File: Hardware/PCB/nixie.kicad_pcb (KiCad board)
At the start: 4 copper layers, 241.3 x 116.8 mm, 329 parts, among them J101 USB_B, J102 Conn_01x10, J103 PT100 1, J104 PT100 2, J105 DCF77 Antenna, J201 Hr_Ten, J202 Hr_One, J203 Min_dot, J204 Min_Ten, J205 Min_One, J206 Min_dot, J207 Sec_Ten, J208 Sec_One, J301 Sec_One, J302 Sec_Ten, J303 Min_One, J304 Min_Ten, J305 Hr_One, J306 Hr_Ten, J307 Sec_Dec, J308 Sec_Dec, J401 Barrel_Jack, Q101 BC546, Q102 BC546, Q103 BC546, Q104 BC546, Q301 MPSA92, Q302 MPSA42, Q303 MPSA42, Q304 MPSA42, Q305 MPSA42, Q306 MPSA42, Q307 MPSA42, Q308 MPSA42, Q309 MPSA42, Q310 MPSA42, Q311 MPSA42, Q312 MPSA42, Q313 MPSA42, Q314 MPSA42, Q315 MPSA42, Q316 MPSA42, Q317 MPSA42, Q318 MPSA42, Q319 MPSA92, Q320 MPSA42, Q321 MPSA42, Q322 MPSA42, Q323 MPSA42, Q324 MPSA42, Q325 MPSA42, Q326 MPSA42, Q327 MPSA42, Q328 MPSA42, Q329 MPSA42, Q330 MPSA42, Q331 MPSA42, Q332 MPSA42, Q333 MPSA42, Q334 MPSA42, Q335 MPSA42, Q336 MPSA42, Q337 MPSA92, Q338 MPSA42, Q339 MPSA92, Q340 MPSA42, Q341 MPSA42, Q342 MPSA42, Q343 MPSA42, Q344 MPSA42, Q345 MPSA42, Q346 MPSA42, Q347 MPSA42, Q348 MPSA42, Q349 MPSA42, Q350 MPSA42, Q351 MPSA42, Q352 MPSA42, Q353 MPSA42, Q354 MPSA42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

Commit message: PCB update finished placing and routing Cleanup Passes need to be done Silkscreen needs to be done
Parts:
- removed JP101: VBUS Jumper, Connector_PinHeader_2.54mm:PinHeader_1x02_P2.54mm_Vertical
- removed Q101, Q102: BC546, Package_TO_SOT_THT:TO-92
- removed R106: 100, Resistor_THT:R_Axial_DIN0207_L6.3mm_D2.5mm_P2.54mm_Vertical
- removed RN102: R_Network08, Resistor_THT:R_Array_SIP9
- removed SW106, SW107, SW108, SW109: SW_SPST, Button_Switch_THT:SW_SPST_Omron_B3F-315x_Angled
- removed SW110: BOOT, Button_Switch_SMD:SW_Tactile_SPST_NO_Straight_CK_PTS636Sx25SMTRLFS
- removed SW111: RST, Button_Switch_SMD:SW_Tactile_SPST_NO_Straight_CK_PTS636Sx25SMTRLFS
- added G***: LOGO, Eigene:logo, F.Cu at (168.8, 55.9)
- added Q1: BC846, Package_TO_SOT_SMD:SOT-23, F.Cu at (138.7, 63.0)
- added Q2: BC846, Package_TO_SOT_SMD:SOT-23, F.Cu at (138.7, 59.6)
- added REF**: ESD-Logo_8.9x8mm_SilkScreen, Symbol:ESD-Logo_8.9x8mm_SilkScreen, F.Cu at (155.3, 53.7)
- added REF**: WEEE-Logo_5.6x8mm_SilkScreen, Symbol:WEEE-Logo_5.6x8mm_SilkScreen, F.Cu at (25.9, 44.7)
- added REF**: Symbol_HighVoltage_Triangle_8x7mm_Copper, Symbol:Symbol_HighVoltage_Triangle_8x7mm_Copper, F.Cu at (26.0, 54.0)
- added REF**: OSHW-Logo2_9.8x8mm_SilkScreen, Symbol:OSHW-Logo2_9.8x8mm_SilkScreen, F.Cu at (146.2, 53.6)
- added RN1: 10k, Resistor_THT:R_Array_SIP5, F.Cu at (221.9, 63.5)
- added Ref**: Val**, Eigene:ladder_4, F.Cu at (31.9, 84.6)
- added TP1: TestPoint, Connector_Pin:Pin_D1.0mm_L10.0mm, F.Cu at (209.9, 77.9)
- added TP2: TestPoint, Connector_Pin:Pin_D1.0mm_L10.0mm, F.Cu at (214.0, 77.9)
- added TP3: TestPoint, Connector_Pin:Pin_D1.0mm_L10.0mm, F.Cu at (218.0, 77.9)
- added TP4: TestPoint, Connector_Pin:Pin_D1.0mm_L10.0mm, F.Cu at (222.1, 77.9)
- C101, C102, C104, C105: footprint Capacitor_THT:C_Disc_D3.0mm_W1.6mm_P2.50mm -> Capacitor_SMD:C_0805_2012Metric
- D401, D402, D403: value 1N4007 -> UF4007
- J103, J104: footprint Connector_JST:JST_XH_B2B-XH-A_1x02_P2.50mm_Vertical -> Connector_PinHeader_2.54mm:PinHeader_1x02_P2.54mm_Vertical
- R101: footprint Resistor_THT:R_Axial_DIN0207_L6.3mm_D2.5mm_P7.62mm_Horizontal -> Resistor_SMD:R_0805_2012Metric
- R102, R103, R104, R105, R107, R108, R109: footprint Resistor_THT:R_Axial_DIN0207_L6.3mm_D2.5mm_P2.54mm_Vertical -> Resistor_SMD:R_0805_2012Metric
- R303, R343: footprint Resistor_THT:R_Axial_DIN0207_L6.3mm_D2.5mm_P2.54mm_Vertical -> Resistor_THT:R_Axial_DIN0207_L6.3mm_D2.5mm_P7.62mm_Horizontal
- U103: footprint Package_DFN_QFN:QFN-28-1EP_5x5mm_P0.5mm_EP3.35x3.35mm -> Package_DFN_QFN:QFN-28-1EP_5x5mm_P0.5mm_EP3.35x3.35mm_ThermalVias
- moved U102 239.5 mm to (121.2, 60.2), turned to -90 degrees
- moved C101 228.8 mm to (123.1, 64.8)
- moved U103 228.2 mm to (130.2, 61.2), turned to -90 degrees
- moved C102 226.3 mm to (124.0, 59.8), turned to -90 degrees
- moved FB101 216.2 mm to (127.0, 67.4)
- moved R101 214.5 mm to (126.0, 59.8), turned to -90 degrees
- moved J101 199.7 mm to (131.4, 70.9), turned to -90 degrees
- moved R102 198.5 mm to (135.8, 63.0), turned to 90 degrees
- moved R103 196.8 mm to (135.8, 59.6), turned to 90 degrees
- moved J104 195.4 mm to (180.2, 81.9)
- moved J103 192.4 mm to (184.0, 81.9)
- moved R107 191.0 mm to (148.6, 58.9), turned to 180 degrees
- moved R104 190.9 mm to (141.6, 63.0), turned to -90 degrees
- moved R105 189.5 mm to (141.6, 59.6), turned to -90 degrees
- moved J105 188.6 mm to (174.8, 84.5), turned to -90 degrees
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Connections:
- net /Dm renamed /D-
- net /Dp renamed /D+
- net Net-(J101-D+) renamed /DP
- net Net-(J101-D-) renamed /DN
- net Net-(J301-Pin_12) renamed /Nixie Driver/Anode1
- net Net-(J302-Pin_12) renamed /Nixie Driver/Anode2
- net Net-(J303-Pin_12) renamed /Nixie Driver/Anode3
- net Net-(J304-Pin_12) renamed /Nixie Driver/Anode4
- net Net-(J305-Pin_12) renamed /Nixie Driver/Anode5
- net Net-(J306-Pin_12) renamed /Nixie Driver/Anode6
- net Net-(J307-Pin_4) renamed /Nixie Driver/Anode7
- net Net-(J308-Pin_4) renamed /Nixie Driver/Anode8
- FB101 pad 1: Net-(JP101-B) -> Net-(J101-VBUS)
- R303 pad 1: /Nixie Driver/A0 -> /A0
- R323 pad 1: /Nixie Driver/A1 -> /A1
- R343 pad 1: /Nixie Driver/A2 -> /A3
- R347 pad 1: /Nixie Driver/A3 -> /A4
- R367 pad 1: /Nixie Driver/A4 -> /A6
- R387 pad 1: /Nixie Driver/A5 -> /A7
- R393 pad 2: /Nixie Driver/A6 -> /A2
- R398 pad 2: /Nixie Driver/A7 -> /A5
- SW101 pad 1: Net-(RN101-R1) -> GND
- SW101 pad 10: GND -> Net-(RN101-R7)
- SW101 pad 11: GND -> Net-(RN101-R6)
- SW101 pad 12: GND -> Net-(RN101-R5)
- SW101 pad 13: GND -> Net-(RN101-R4)
- SW101 pad 14: GND -> Net-(RN101-R3)
- SW101 pad 15: GND -> Net-(RN101-R2)
- SW101 pad 16: GND -> Net-(RN101-R1)
- SW101 pad 2: Net-(RN101-R2) -> GND
- SW101 pad 3: Net-(RN101-R3) -> GND
- SW101 pad 4: Net-(RN101-R4) -> GND
- SW101 pad 5: Net-(RN101-R5) -> GND
- SW101 pad 6: Net-(RN101-R6) -> GND
- SW101 pad 7: Net-(RN101-R7) -> GND
- SW101 pad 8: Net-(RN101-R8) -> GND
- SW101 pad 9: GND -> Net-(RN101-R8)
- U105 pad 12: SDA -> I/O
- U105 pad 13: /A0 -> /SCLK
- U105 pad 14: /SCLK -> /DAT
- U105 pad 16: /~{SCLR} -> /RCLK
- U105 pad 23: /A1 -> /~{SCLR}
- U105 pad 26: /DAT -> INT
- U105 pad 27: /A2 -> /A0
- U105 pad 28: /A3 -> /A1
- U105 pad 29: /RCLK -> /A2
- U105 pad 30: /A4 -> /A3
- U105 pad 31: /A5 -> /A4
- U105 pad 33: /A6 -> /A5
- U105 pad 36: /A7 -> /A6
- U105 pad 37: I/O -> /A7
- U105 pad 6: DCF_EN -> SDA
- U105 pad 7: DCF_SIG -> SCL
- U105 pad 8: SCL -> DCF_SIG
- U105 pad 9: INT -> DCF_EN
- U301 pad 10: /Nixie Driver/~{SCLR} -> /~{SCLR}
- U301 pad 11: /Nixie Driver/SCLK -> /SCLK
- U301 pad 12: /Nixie Driver/RCLK -> /RCLK
- U301 pad 14: /Nixie Driver/DAT -> /DAT
- U302 pad 10: /Nixie Driver/~{SCLR} -> /~{SCLR}
- U302 pad 11: /Nixie Driver/SCLK -> /SCLK
- U302 pad 12: /Nixie Driver/RCLK -> /RCLK
- U303 pad 10: /Nixie Driver/~{SCLR} -> /~{SCLR}
- U303 pad 11: /Nixie Driver/SCLK -> /SCLK
- U303 pad 12: /Nixie Driver/RCLK -> /RCLK
- U304 pad 10: /Nixie Driver/~{SCLR} -> /~{SCLR}
- U304 pad 11: /Nixie Driver/SCLK -> /SCLK
- U304 pad 12: /Nixie Driver/RCLK -> /RCLK
- U305 pad 10: /Nixie Driver/~{SCLR} -> /~{SCLR}
- U305 pad 11: /Nixie Driver/SCLK -> /SCLK
- U305 pad 12: /Nixie Driver/RCLK -> /RCLK
- U306 pad 10: /Nixie Driver/~{SCLR} -> /~{SCLR}
- U306 pad 11: /Nixie Driver/SCLK -> /SCLK
- U306 pad 12: /Nixie Driver/RCLK -> /RCLK
- U307 pad 10: /Nixie Driver/~{SCLR} -> /~{SCLR}
- U307 pad 11: /Nixie Driver/SCLK -> /SCLK
- U307 pad 12: /Nixie Driver/RCLK -> /RCLK
- U308 pad 10: /Nixie Driver/~{SCLR} -> /~{SCLR}
- U308 pad 11: /Nixie Driver/SCLK -> /SCLK
- U308 pad 12: /Nixie Driver/RCLK -> /RCLK
- Y101 pad 2: GND -> Net-(U107-X2)
- Y101 pad 3: Net-(U107-X2) -> GND
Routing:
- net +180V: track 0.00 -> 388.8 mm
- net /~{SCLR}: track 0.00 -> 259.8 mm, vias 0 -> 9
- net /SCLK: track 0.00 -> 259.7 mm, vias 0 -> 9
- net /RCLK: track 0.00 -> 252.1 mm, vias 0 -> 7
- net /A7: track 0.00 -> 129.4 mm, vias 0 -> 2
- net +12V: track 0.00 -> 113.0 mm
- net /A0: track 0.00 -> 107.3 mm, vias 0 -> 2
- net INT: track 0.00 -> 100.9 mm, vias 0 -> 1
- net SCL: track 0.00 -> 97.8 mm, vias 0 -> 4
- net SDA: track 0.00 -> 97.5 mm, vias 0 -> 3
- net /A6: track 0.00 -> 96.8 mm, vias 0 -> 2
- net /DAT: track 0.00 -> 93.1 mm
- net /A1: track 0.00 -> 83.4 mm, vias 0 -> 1
- net +90V: track 0.00 -> 68.0 mm
- net /A5: track 0.00 -> 63.7 mm, vias 0 -> 3
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- added copper zone on In2.Cu, net +3V3
- added copper zone on In1.Cu, net GND
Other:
- board size 241.3 x 116.8 mm -> 240.8 x 153.6 mm
- board text added: "ESP32 Controller Board"
- board text added: "Z5600M Nixie Clock"

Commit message: PCB Update Silkscreen cleanup Layout Cleanup concept front plate
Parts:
- added G***: LOGO, Eigene:logo, F.Cu at (109.0, 163.3)
- added REF**: Symbol_HighVoltage_Triangle_8x7mm_Copper, Symbol:Symbol_HighVoltage_Triangle_8x7mm_Copper, F.Cu at (60.6, 165.2)
- added REF**: ESD-Logo_8.9x8mm_SilkScreen, Symbol:ESD-Logo_8.9x8mm_SilkScreen, F.Cu at (95.1, 164.7)
- added REF**: OSHW-Logo2_9.8x8mm_SilkScreen, Symbol:OSHW-Logo2_9.8x8mm_SilkScreen, F.Cu at (82.3, 165.2)
- added REF**: WEEE-Logo_5.6x8mm_SilkScreen, Symbol:WEEE-Logo_5.6x8mm_SilkScreen, F.Cu at (71.1, 164.7)
- added TP10: TestPoint, Connector_Pin:Pin_D1.0mm_L10.0mm, F.Cu at (143.8, 78.2)
- added TP5: TestPoint, Connector_Pin:Pin_D1.0mm_L10.0mm, F.Cu at (141.0, 67.1)
- added TP6: TestPoint, Connector_Pin:Pin_D1.0mm_L10.0mm, F.Cu at (143.8, 68.6)
- added TP7: TestPoint, Connector_Pin:Pin_D1.0mm_L10.0mm, F.Cu at (141.0, 70.1)
- added TP8: TestPoint, Connector_Pin:Pin_D1.0mm_L10.0mm, F.Cu at (143.8, 71.6)
- added TP9: TestPoint, Connector_Pin:Pin_D1.0mm_L10.0mm, F.Cu at (141.0, 76.7)
- moved Ref** 0.38 mm to (32.3, 84.6)
- moved R367 0.29 mm to (225.2, 48.3)
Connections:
- R323 pad 1: /A1 -> /A0
- R343 pad 1: /A3 -> /A0
- R347 pad 1: /A4 -> /A0
- R367 pad 1: /A6 -> /A0
- R387 pad 1: /A7 -> /A0
- R393 pad 2: /A2 -> /A0
- R398 pad 2: /A5 -> /A0
- U105 pad 28: /A1 -> Net-(U105-IO17)
- U105 pad 30: /A3 -> Net-(U105-IO18)
- U105 pad 31: /A4 -> Net-(U105-IO19)
- U105 pad 33: /A5 -> Net-(U105-IO21)
- U105 pad 36: /A6 -> Net-(U105-IO22)
- U105 pad 37: /A7 -> Net-(U105-IO23)
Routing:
- net /A0: track 107.3 -> 262.6 mm, vias 2 -> 9
- net /A7: track 129.4 -> 0.00 mm, vias 2 -> 0
- net /A6: track 96.8 -> 0.00 mm, vias 2 -> 0
- net /A1: track 83.4 -> 0.00 mm, vias 1 -> 0
- net +90V: track 68.0 -> 0.00 mm
- net /A5: track 63.7 -> 0.00 mm, vias 3 -> 0
- net /A2: track 58.4 -> 0.00 mm, vias 2 -> 0
- net /A4: track 45.5 -> 0.00 mm, vias 4 -> 0
- net /A3: track 26.1 -> 0.00 mm, vias 2 -> 0
- net Net-(U404-Ipk): track 32.7 -> 8.67 mm
- net Net-(D403-A): track 15.6 -> 0.00 mm
- net Net-(D401-K): track 12.5 -> 0.00 mm
- net Net-(U105-IO17): track 0.00 -> 6.03 mm
- net Net-(U105-IO22): track 0.00 -> 5.82 mm
- net Net-(U105-IO19): track 0.00 -> 5.71 mm
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- added copper zone on F.Cu, net +90V
- added copper zone on F.Cu, net Net-(D401-K)
- added copper zone on F.Cu, net Net-(D403-A)
- added copper zone on F.Cu, net Net-(U404-Ipk)
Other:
- board text added: "3V3 GND SIG EN"
- board text added: "3V3 O1 O2 O3 O4 O5 O6 O7 O8 GND"
- board text added: "ADC1"
- board text added: "ADC2"
- board text added: "Analog"
- board text added: "CONF"
- board text added: "DAY"
- board text added: "DCF77"
- board text added: "DIMM"
- board text added: "Digital Out"
- board text added: "Enter"
- board text added: "HOUR"
- board text added: "LDR2"
- board text added: "MINUTE"
- board text added: "MODE"
- board text added: "MONTH"
- board text added: "NTP"
- board text added: "RTC"
- board text added: "SECOND"
- board text added: "T1"
- board text added: "T2"
- board text added: "USB"
- board text added: "YEAR"
- board text added: "https://github.com/Synthron/Nixie"

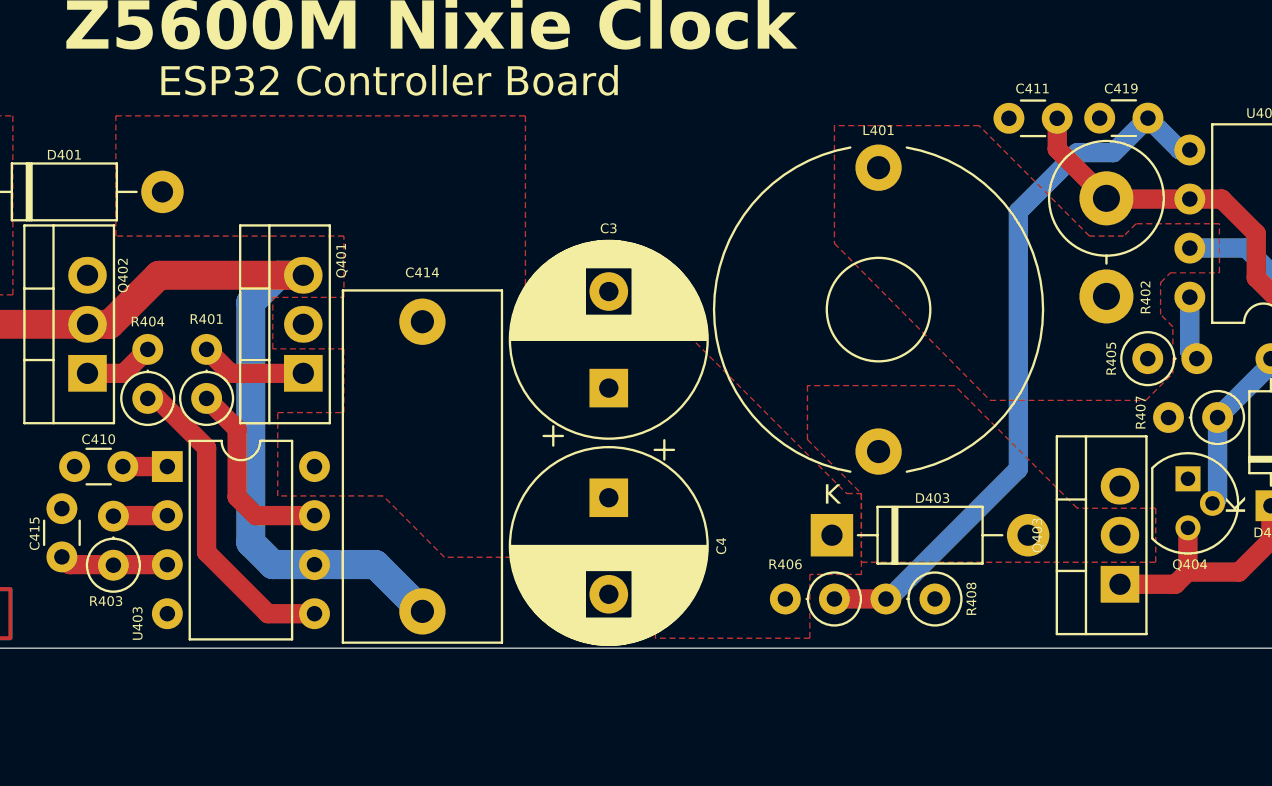
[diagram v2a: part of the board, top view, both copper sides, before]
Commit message: small bugfix update
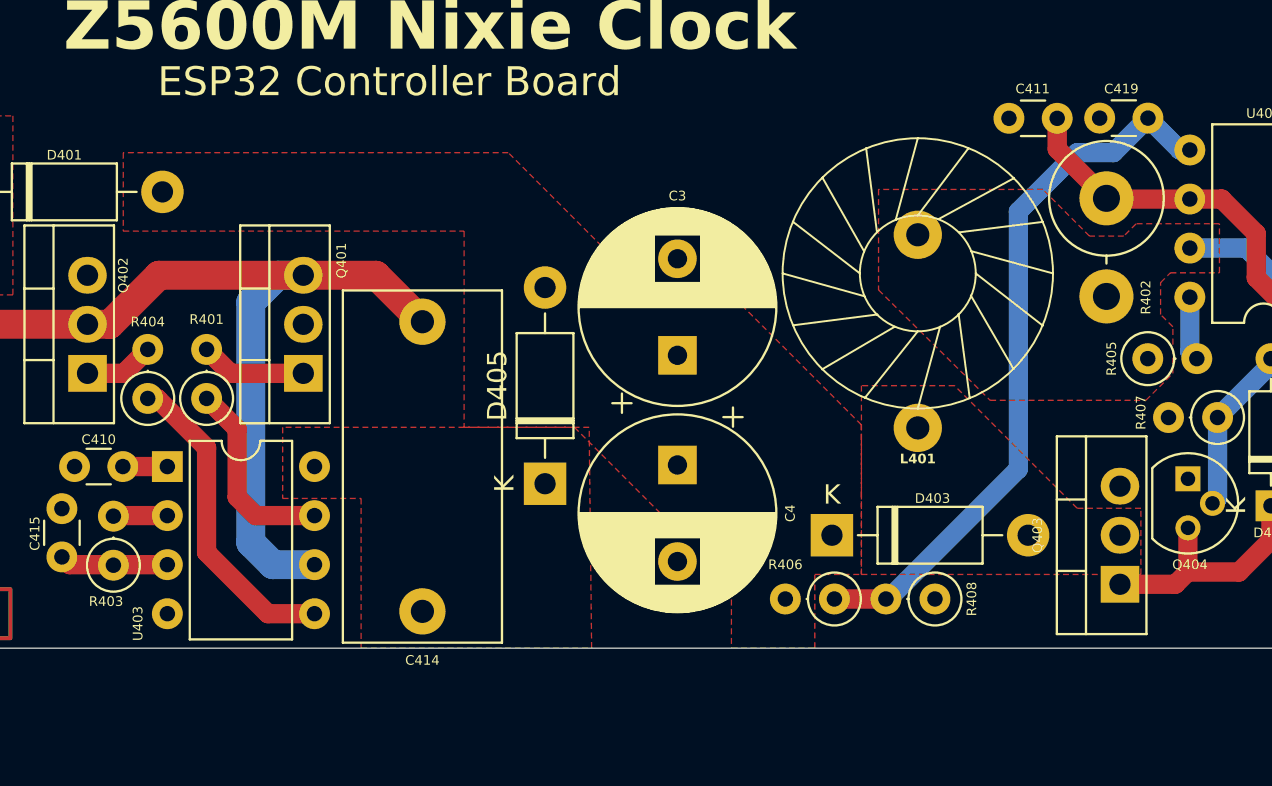
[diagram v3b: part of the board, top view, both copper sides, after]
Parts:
- added D405: UF4007, Diode_THT:D_DO-41_SOD81_P10.16mm_Horizontal, F.Cu at (65.0, 77.9)
- L401: footprint Inductor_THT:L_Toroid_Horizontal_D16.8mm_P14.70mm_Vishay_TJ3 -> Inductor_THT:L_Toroid_Horizontal_D6.5mm_P10.00mm_Diameter7-5mm_Amidon-T25
- moved C414 15.0 mm to (58.7, 84.5), turned to 90 degrees
- moved L401 4.03 mm to (84.3, 65.0)
- moved C3 3.94 mm to (71.9, 71.2)
- moved C4 3.94 mm to (71.9, 76.9)
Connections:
- C414 pad 1: +90V -> Net-(D405-K)
- U403 pad 8: +90V -> Net-(D405-K)
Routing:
- net +90V: track 0.00 -> 11.7 mm
- net Net-(Q401-S): track 54.5 -> 55.1 mm
- added copper zone on F.Cu, net Net-(D405-K)
